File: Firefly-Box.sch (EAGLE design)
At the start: 35 parts, among them J1 USB MICRO, U1 ATMEGA32U4-XUMU, U2 ATMEGA32U4-XUAU, Y1 16MHz KX-7

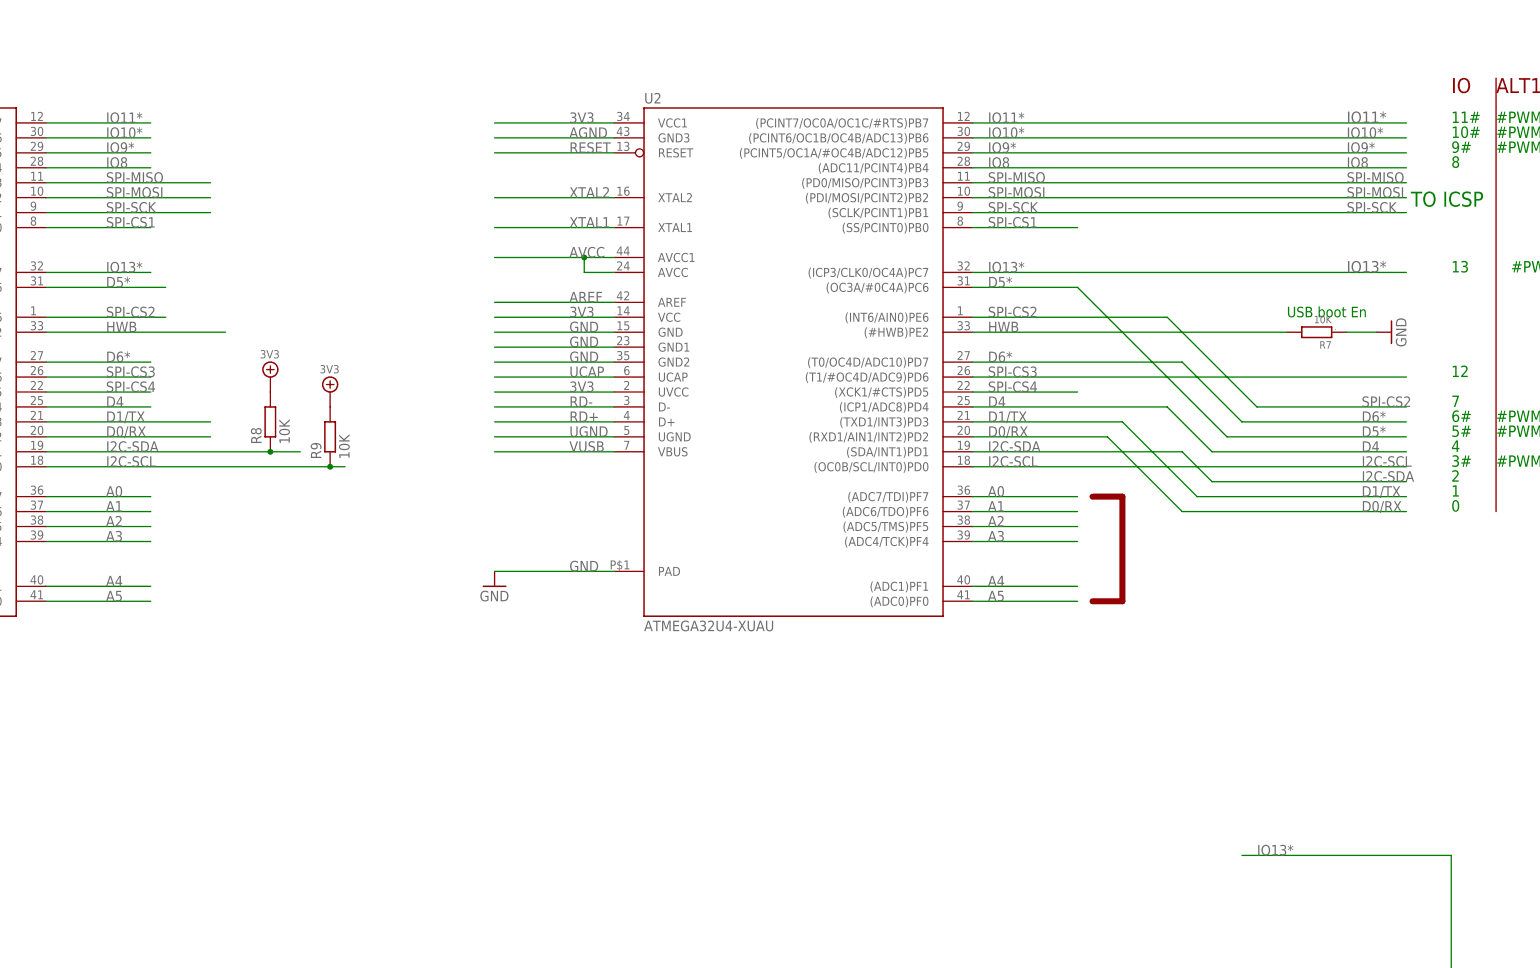
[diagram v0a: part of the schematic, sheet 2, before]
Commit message: Fixed pin names
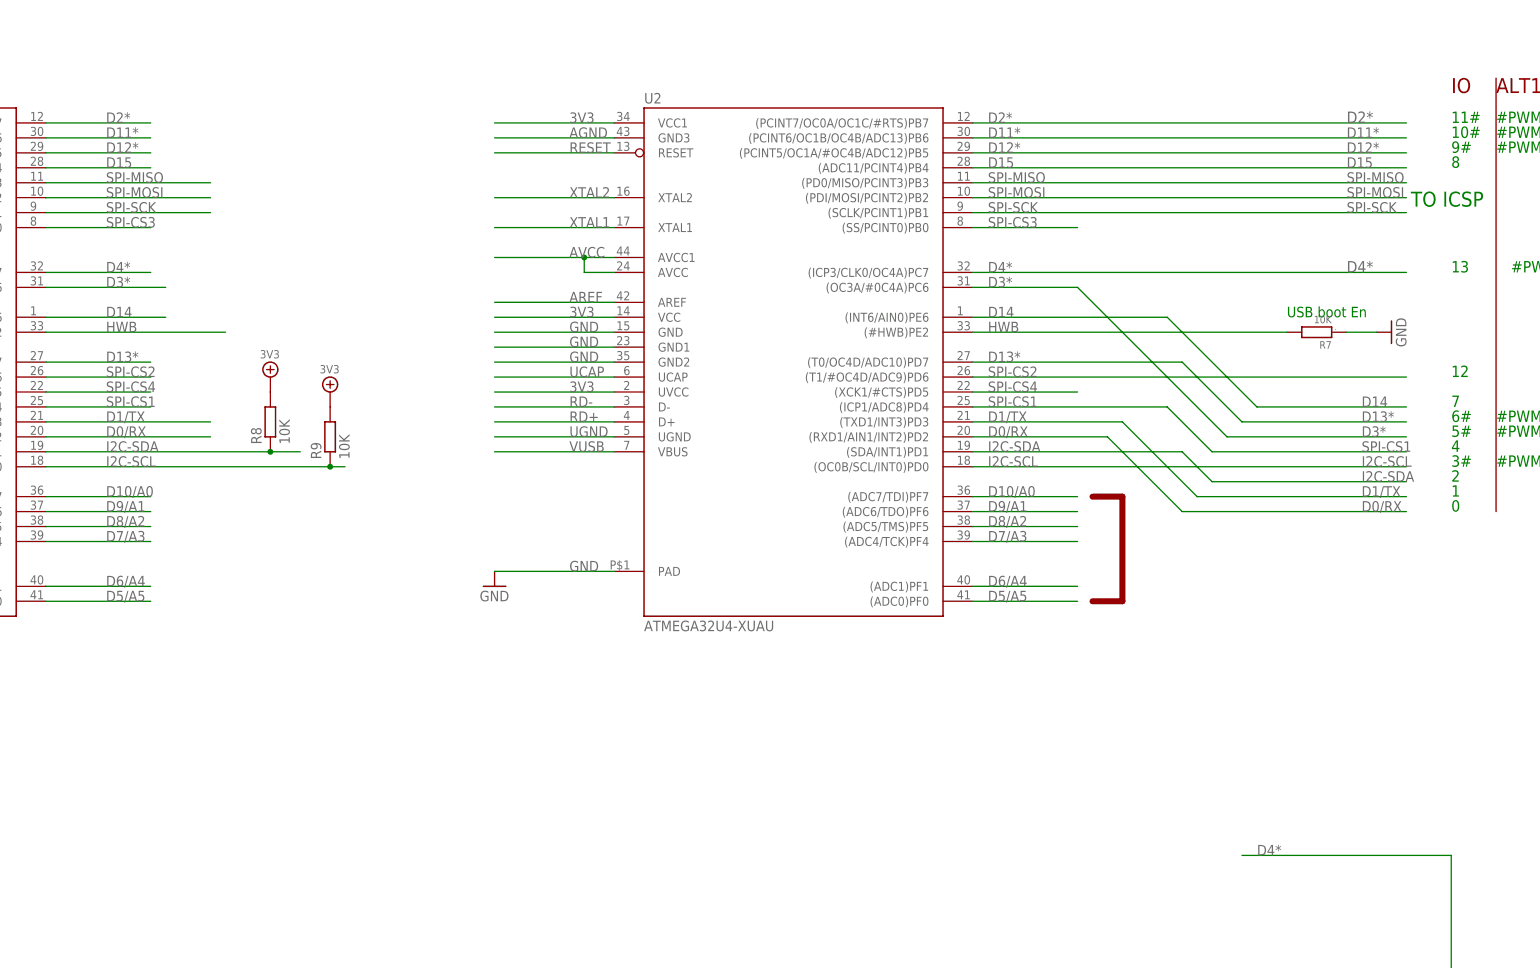
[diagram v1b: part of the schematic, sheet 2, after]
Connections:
- net A0 renamed D10/A0
- net A1 renamed D9/A1
- net A2 renamed D8/A2
- net A3 renamed D7/A3
- net A4 renamed D6/A4
- net A5 renamed D5/A5
- net D5* renamed D3*
- net D6* renamed D13*
- net IO10* renamed D11*
- net IO11* renamed D2*
- net IO13* renamed D4*
- net IO8 renamed D15
- net IO9* renamed D12*
- removed net D4: BUS1.4, U1.(ICP1/ADC8)PD4, U2.(ICP1/ADC8)PD4
- removed net N$25: BUS3.5
- removed net N$26: BUS3.6
- removed net N$33: BUS4.5
- removed net N$34: BUS4.6
- removed net N$48: BUS2.5
- removed net NC: BUS1.6
- removed net NC2: BUS1.5
- removed net NC3: BUS2.6
- new net D14: AH1.7, AH2.2, U1.(INT6/AIN0)PE6, U2.(INT6/AIN0)PE6
- net SPI-CS1: now also BUS1.4, U1.(ICP1/ADC8)PD4, U2.(ICP1/ADC8)PD4; no longer BUS3.4, U1.(SS/PCINT0)PB0, U2.(SS/PCINT0)PB0
- net SPI-CS2: now also BUS2.4, U1.(T1/#OC4D/ADC9)PD6, U2.(T1/#OC4D/ADC9)PD6; no longer AH1.7, AH2.2, U1.(INT6/AIN0)PE6, U2.(INT6/AIN0)PE6
- net SPI-CS3: now also BUS3.4, U1.(SS/PCINT0)PB0, U2.(SS/PCINT0)PB0; no longer BUS2.4, U1.(T1/#OC4D/ADC9)PD6, U2.(T1/#OC4D/ADC9)PD6
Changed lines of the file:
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@@
 </segment>
 </net>
-<net name="IO11*" class="0">
+<net name="D2*" class="0">
 <segment>
 <pinref part="AL1" gate="G$1" pin="3"/>
@@
 </segment>
 </net>
-<net name="IO9*" class="0">
+<net name="D12*" class="0">
 <segment>
 <pinref part="AH1" gate="G$1" pin="5"/>
@@
 </segment>
 </net>
-<net name="A0" class="0">
+<net name="D10/A0" class="0">
 <segment>
 <pinref part="AH1" gate="G$1" pin="3"/>
@@
 </segment>
 </net>
-<net name="A1" class="0">
+<net name="D9/A1" class="0">
 <segment>
 <pinref part="AH1" gate="G$1" pin="2"/>
@@
 </segment>
 </net>
-<net name="A2" class="0">
+<net name="D8/A2" class="0">
 <segment>
 <pinref part="AH1" gate="G$1" pin="1"/>
@@
 </segment>
 </net>
-<net name="IO8" class="0">
+<net name="D15" class="0">
 <segment>
 <pinref part="AH1" gate="G$1" pin="8"/>
@@
 </segment>
 </net>
-<net name="N$25" class="0">
-<segment>
-<pinref part="BUS3" gate="G$1" pin="5"/>
-<wire x1="193.04" y1="127" x2="193.04" y2="134.62" width="0.2032" layer="91"/>
-<label x="193.04" y="127" size="1.778" layer="95" rot="R90"/>
-</segment>
-</net>
-<net name="N$26" class="0">
-<segment>
-<pinref part="BUS3" gate="G$1" pin="6"/>
-<wire x1="195.58" y1="127" x2="195.58" y2="134.62" width="0.2032" layer="91"/>
-<label x="195.58" y="127" size="1.778" layer="95" rot="R90"/>
-</segment>
-</net>
 <net name="I2C-SCL" class="0">
 <segment>
@@
 </segment>
 </net>
-<net name="N$33" class="0">
-<segment>
-<pinref part="BUS4" gate="G$1" pin="5"/>
-<wire x1="215.9" y1="127" x2="215.9" y2="134.62" width="0.2032" layer="91"/>
-<label x="215.9" y="127" size="1.778" layer="95" rot="R90"/>
-</segment>
-</net>
-<net name="N$34" class="0">
-<segment>
-<pinref part="BUS4" gate="G$1" pin="6"/>
-<wire x1="218.44" y1="127" x2="218.44" y2="134.62" width="0.2032" layer="91"/>
-<label x="218.44" y="127" size="1.778" layer="95" rot="R90"/>
-</segment>
-</net>
 <net name="I2C-SDA" class="0">
 <segment>
@@
 </segment>
 </net>
-<net name="N$48" class="0">
-<segment>
-<pinref part="BUS2" gate="G$1" pin="5"/>
-<wire x1="68.58" y1="66.04" x2="68.58" y2="53.34" width="0.2032" layer="91"/>
-<label x="68.58" y="53.34" size="1.778" layer="95" rot="R90"/>
-</segment>
-</net>
-<net name="NC" class="0">
-<segment>
-<pinref part="BUS1" gate="G$1" pin="6"/>
-<wire x1="43.18" y1="66.04" x2="43.18" y2="53.34" width="0.2032" layer="91"/>
-<label x="43.18" y="53.34" size="1.778" layer="95" rot="R90"/>
-</segment>
-</net>
-<net name="NC2" class="0">
-<segment>
-<pinref part="BUS1" gate="G$1" pin="5"/>
-<wire x1="45.72" y1="66.04" x2="45.72" y2="53.34" width="0.2032" layer="91"/>
-<label x="45.72" y="53.34" size="1.778" layer="95" rot="R90"/>
-</segment>
-</net>
-<net name="A3" class="0">
+<net name="D7/A3" class="0">
 <segment>
 <pinref part="AL1" gate="G$1" pin="8"/>
@@
 </segment>
 </net>
-<net name="A4" class="0">
+<net name="D6/A4" class="0">
 <segment>
 <pinref part="AL1" gate="G$1" pin="7"/>
@@
 </segment>
 </net>
-<net name="A5" class="0">
+<net name="D5/A5" class="0">
 <segment>
 <pinref part="AL1" gate="G$1" pin="6"/>
@@
 </segment>
 </net>
-<net name="D6*" class="0">
+<net name="D13*" class="0">
 <segment>
 <pinref part="AH1" gate="G$1" pin="6"/>
@@
 </segment>
 </net>
-<net name="D5*" class="0">
+<net name="D3*" class="0">
 <segment>
 <pinref part="AL1" gate="G$1" pin="4"/>
@@
 </segment>
 </net>
-<net name="IO10*" class="0">
+<net name="D4*" class="0">
+<segment>
+<pinref part="AL1" gate="G$1" pin="5"/>
+<pinref part="AL2" gate="G$1" pin="4"/>
+<wire x1="129.54" y1="109.22" x2="139.7" y2="109.22" width="0.2032" layer="91"/>
+<label x="129.54" y="109.22" size="1.778" layer="95"/>
+</segment>
+</net>
+<net name="SPI-CS3" class="0">
+<segment>
+<pinref part="BUS3" gate="G$1" pin="4"/>
+<wire x1="190.5" y1="127" x2="190.5" y2="134.62" width="0.2032" layer="91"/>
+<label x="190.5" y="127" size="1.778" layer="95" rot="R90"/>
+</segment>
+</net>
+<net name="SPI-CS1" class="0">
+<segment>
+<pinref part="BUS1" gate="G$1" pin="4"/>
+<wire x1="48.26" y1="66.04" x2="48.26" y2="53.34" width="0.2032" layer="91"/>
+<label x="48.26" y="53.34" size="1.778" layer="95" rot="R90"/>
+</segment>
+</net>
+<net name="SPI-CS2" class="0">
+<segment>
+<pinref part="BUS2" gate="G$1" pin="4"/>
+<wire x1="71.12" y1="66.04" x2="71.12" y2="53.34" width="0.2032" layer="91"/>
+<label x="71.12" y="53.34" size="1.778" layer="95" rot="R90"/>
+</segment>
+</net>
+<net name="D14" class="0">
+<segment>
+<pinref part="AH1" gate="G$1" pin="7"/>
+<pinref part="AH2" gate="G$1" pin="2"/>
+<wire x1="129.54" y1="81.28" x2="139.7" y2="81.28" width="0.2032" layer="91"/>
+<label x="129.54" y="81.28" size="1.778" layer="95"/>
+</segment>
+</net>
+<net name="D11*" class="0">
 <segment>
 <pinref part="AH1" gate="G$1" pin="4"/>
@@
 <wire x1="129.54" y1="88.9" x2="139.7" y2="88.9" width="0.2032" layer="91"/>
 <label x="129.54" y="88.9" size="1.778" layer="95"/>
-</segment>
-</net>
-<net name="IO13*" class="0">
-<segment>
-<pinref part="AL1" gate="G$1" pin="5"/>
-<pinref part="AL2" gate="G$1" pin="4"/>
-<wire x1="129.54" y1="109.22" x2="139.7" y2="109.22" width="0.2032" layer="91"/>
-<label x="129.54" y="109.22" size="1.778" layer="95"/>
-</segment>
-</net>
-<net name="NC3" class="0">
-<segment>
-<pinref part="BUS2" gate="G$1" pin="6"/>
-<wire x1="66.04" y1="66.04" x2="66.04" y2="53.34" width="0.2032" layer="91"/>
-<label x="66.04" y="53.34" size="1.778" layer="95" rot="R90"/>
-</segment>
-</net>
-<net name="SPI-CS1" class="0">
-<segment>
-<pinref part="BUS3" gate="G$1" pin="4"/>
-<wire x1="190.5" y1="127" x2="190.5" y2="134.62" width="0.2032" layer="91"/>
-<label x="190.5" y="127" size="1.778" layer="95" rot="R90"/>
-</segment>
-</net>
-<net name="D4" class="0">
-<segment>
-<pinref part="BUS1" gate="G$1" pin="4"/>
-<wire x1="48.26" y1="66.04" x2="48.26" y2="53.34" width="0.2032" layer="91"/>
-<label x="48.26" y="53.34" size="1.778" layer="95" rot="R90"/>
-</segment>
-</net>
-<net name="SPI-CS3" class="0">
-<segment>
-<pinref part="BUS2" gate="G$1" pin="4"/>
-<wire x1="71.12" y1="66.04" x2="71.12" y2="53.34" width="0.2032" layer="91"/>
-<label x="71.12" y="53.34" size="1.778" layer="95" rot="R90"/>
-</segment>
-</net>
-<net name="SPI-CS2" class="0">
-<segment>
-<pinref part="AH1" gate="G$1" pin="7"/>
-<pinref part="AH2" gate="G$1" pin="2"/>
-<wire x1="129.54" y1="81.28" x2="139.7" y2="81.28" width="0.2032" layer="91"/>
-<label x="129.54" y="81.28" size="1.778" layer="95"/>
 </segment>
 </net>
@@
 </segment>
 </net>
-<net name="SPI-CS3" class="0">
+<net name="SPI-CS2" class="0">
 <segment>
 <wire x1="71.12" y1="83.82" x2="53.34" y2="83.82" width="0.1524" layer="91"/>
@@
 </segment>
 </net>
-<net name="IO11*" class="0">
+<net name="D2*" class="0">
 <segment>
 <wire x1="71.12" y1="127" x2="53.34" y2="127" width="0.1524" layer="91"/>
@@
 </segment>
 </net>
-<net name="IO9*" class="0">
+<net name="D12*" class="0">
 <segment>
 <wire x1="71.12" y1="121.92" x2="53.34" y2="121.92" width="0.1524" layer="91"/>
@@
 </segment>
 </net>
-<net name="IO10*" class="0">
+<net name="D11*" class="0">
 <segment>
 <wire x1="71.12" y1="124.46" x2="53.34" y2="124.46" width="0.1524" layer="91"/>
@@
 </segment>
 </net>
-<net name="A3" class="0">
+<net name="D7/A3" class="0">
 <segment>
 <wire x1="53.34" y1="55.88" x2="71.12" y2="55.88" width="0.1524" layer="91"/>
@@
 </segment>
 </net>
-<net name="A2" class="0">
+<net name="D8/A2" class="0">
 <segment>
 <wire x1="53.34" y1="58.42" x2="71.12" y2="58.42" width="0.1524" layer="91"/>
@@
 </segment>
 </net>
-<net name="A1" class="0">
+<net name="D9/A1" class="0">
 <segment>
 <wire x1="53.34" y1="60.96" x2="71.12" y2="60.96" width="0.1524" layer="91"/>
@@
 </segment>
 </net>
-<net name="A0" class="0">
+<net name="D10/A0" class="0">
 <segment>
 <wire x1="53.34" y1="63.5" x2="71.12" y2="63.5" width="0.1524" layer="91"/>
@@
 </segment>
 </net>
-<net name="A4" class="0">
+<net name="D6/A4" class="0">
 <segment>
 <wire x1="53.34" y1="48.26" x2="71.12" y2="48.26" width="0.1524" layer="91"/>
@@
 </segment>
 </net>
-<net name="A5" class="0">
+<net name="D5/A5" class="0">
 <segment>
 <wire x1="53.34" y1="45.72" x2="71.12" y2="45.72" width="0.1524" layer="91"/>
@@
 </segment>
 </net>
-<net name="D5*" class="0">
+<net name="D3*" class="0">
 <segment>
 <wire x1="254" y1="73.66" x2="284.48" y2="73.66" width="0.1524" layer="91"/>
@@
 </segment>
 </net>
-<net name="SPI-CS1" class="0">
+<net name="SPI-CS3" class="0">
 <segment>
 <wire x1="53.34" y1="109.22" x2="71.12" y2="109.22" width="0.1524" layer="91"/>
@@
 </segment>
 </net>
-<net name="D6*" class="0">
+<net name="D13*" class="0">
 <segment>
 <wire x1="71.12" y1="86.36" x2="53.34" y2="86.36" width="0.1524" layer="91"/>
@@
 </segment>
 </net>
-<net name="IO13*" class="0">
+<net name="D4*" class="0">
 <segment>
 <wire x1="256.54" y1="2.54" x2="292.1" y2="2.54" width="0.1524" layer="91"/>
@@
 </segment>
 </net>
-<net name="IO8" class="0">
+<net name="D15" class="0">
 <segment>
 <wire x1="53.34" y1="119.38" x2="71.12" y2="119.38" width="0.1524" layer="91"/>
@@
 </segment>
 </net>
-<net name="SPI-CS2" class="0">
+<net name="D14" class="0">
 <segment>
 <wire x1="259.08" y1="78.74" x2="284.48" y2="78.74" width="0.1524" layer="91"/>
@@
 </segment>
 </net>
-<net name="D4" class="0">
+<net name="SPI-CS1" class="0">
 <segment>
 <wire x1="210.82" y1="78.74" x2="243.84" y2="78.74" width="0.1524" layer="91"/>
